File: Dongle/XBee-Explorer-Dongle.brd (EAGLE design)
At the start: 40.6 x 27.9 mm, 26 parts, among them U1 FT232RL-BASICSSOP, U2 XBEE-1B3, U3 V_REG_LDOSMD

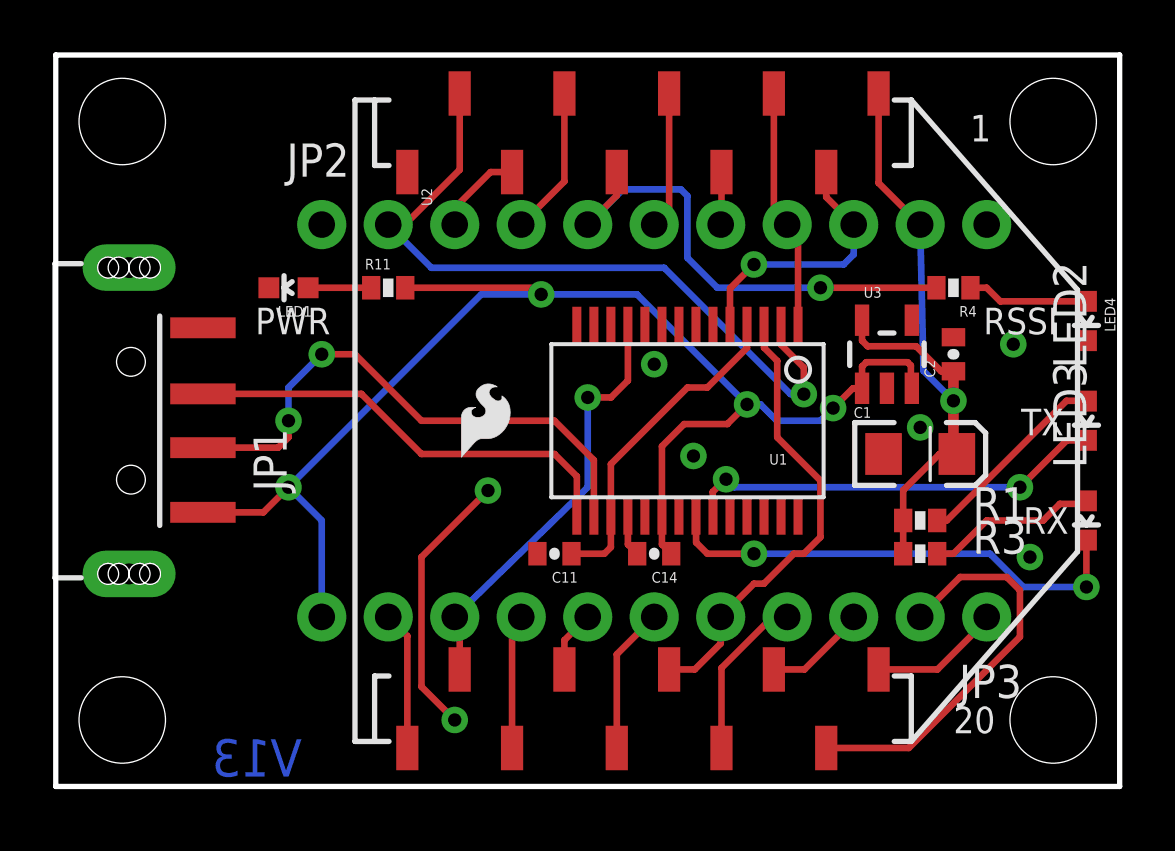
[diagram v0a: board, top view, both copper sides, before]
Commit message: XBee Dongle transition to FT231X
FT231X replaces the FT232RL.
Additional components added (R2, R5, C3, C4).
Updated all resistor and capacitor packages to 0603 footprints.
Rearranged Vreg circuit layout.
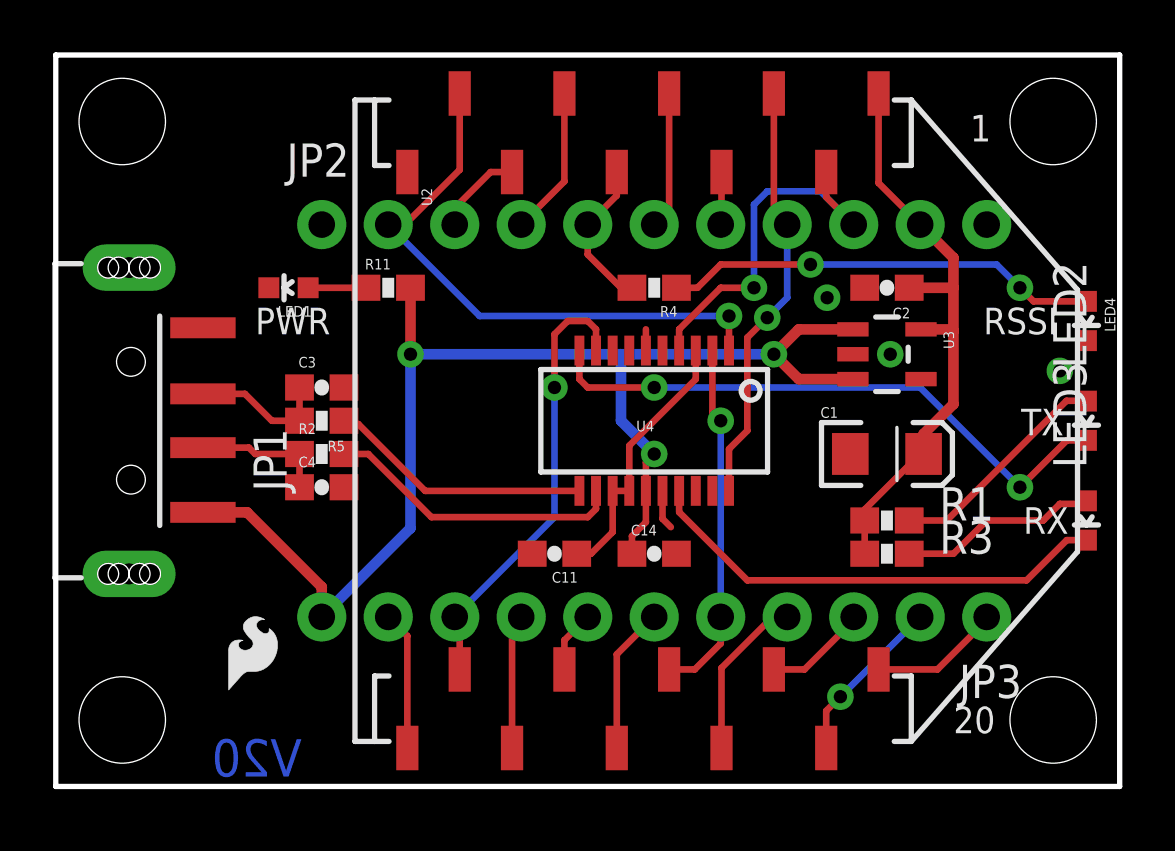
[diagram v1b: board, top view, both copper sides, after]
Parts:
- removed U1: FT232RL-BASICSSOP, SparkFun:SSOP28DB
- added C3, C4: 47pF, SparkFun:0603-CAP
- added R2, R5: 27, SparkFun:0603-RES
- added U4: FT231XS, SparkFun-DigitalIC:SSOP20_L
- C11, C14, C2: device SparkFun:0402-CAP -> SparkFun:0603-CAP
- LED2: value Red -> Red-TX
- LED3: value Green -> Green-RX
- R1, R11, R3, R4: device SparkFun:0402-RES -> SparkFun:0603-RES
- moved U$1 12.6 mm to (6.60, 3.68)
- moved R4 11.4 mm to (22.9, 19.1)
- moved C2 3.59 mm to (31.8, 19.1), turned to 180 degrees
- moved C1 1.27 mm to (31.8, 12.7)
- moved R1 1.27 mm to (31.8, 10.2)
- moved R3 1.27 mm to (31.8, 8.89)
- turned C14 to 0 degrees
- turned U3 to 270 degrees
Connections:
- new net N$5: R2.2, U4.12
- new net N$6: C3.1, JP1.D+1, R5.2
- net 3V-INT: now also U4.13, U4.14, U4.3; no longer U1.17, U1.4
- net 5V: now also U4.15; no longer U1.20
- net CTS: now also U4.9; no longer U1.11
- net DIN: now also U4.20; no longer U1.1
- net DOUT: now also U4.4; no longer U1.5
- net DTR: now also U4.1; no longer U1.2
- net GND: now also C3.2, C4.2, U4.16, U4.6; no longer U1.18, U1.21, U1.25, U1.26, U1.7
- net N$3: now also C4.1, R2.1; no longer U1.16
- net N$7: now also R5.1, U4.11; no longer JP1.D+1, U1.15
- net RTS: now also U4.2; no longer U1.3
- net RXLED: now also U4.17; no longer U1.22
- net TXLED: now also U4.10; no longer U1.23
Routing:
- net N$3: track 21.4 -> 5.06 mm, vias 2 -> 0
- net RSSI: track 19.3 -> 5.83 mm, vias 1 -> 0
- net N$2: track 4.65 -> 16.6 mm, vias 0 -> 2
- net N$5: track 0.00 -> 11.4 mm
- net GND: track 11.9 -> 2.33 mm, vias 7 -> 3
- net DIO1: track 15.6 -> 6.49 mm, vias 0 -> 1
- net N$7: track 17.2 -> 10.1 mm
- net DIN: track 9.23 -> 16.3 mm, vias 0 -> 1
- net TXLED: track 16.3 -> 22.9 mm
- net DTR: track 28.1 -> 22.3 mm
- net N$6: track 0.00 -> 5.38 mm
- net DOUT: track 10.2 -> 14.5 mm
- net RTS: track 17.5 -> 13.7 mm, vias 0 -> 1
- net 5V: track 53.8 -> 50.0 mm, vias 4 -> 3
- net 3.3V: track 26.0 -> 23.2 mm, vias 1 -> 0
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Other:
- board text added: "V20"
- board text removed: "V13"

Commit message: Spaced out resistors and capacitors a tad
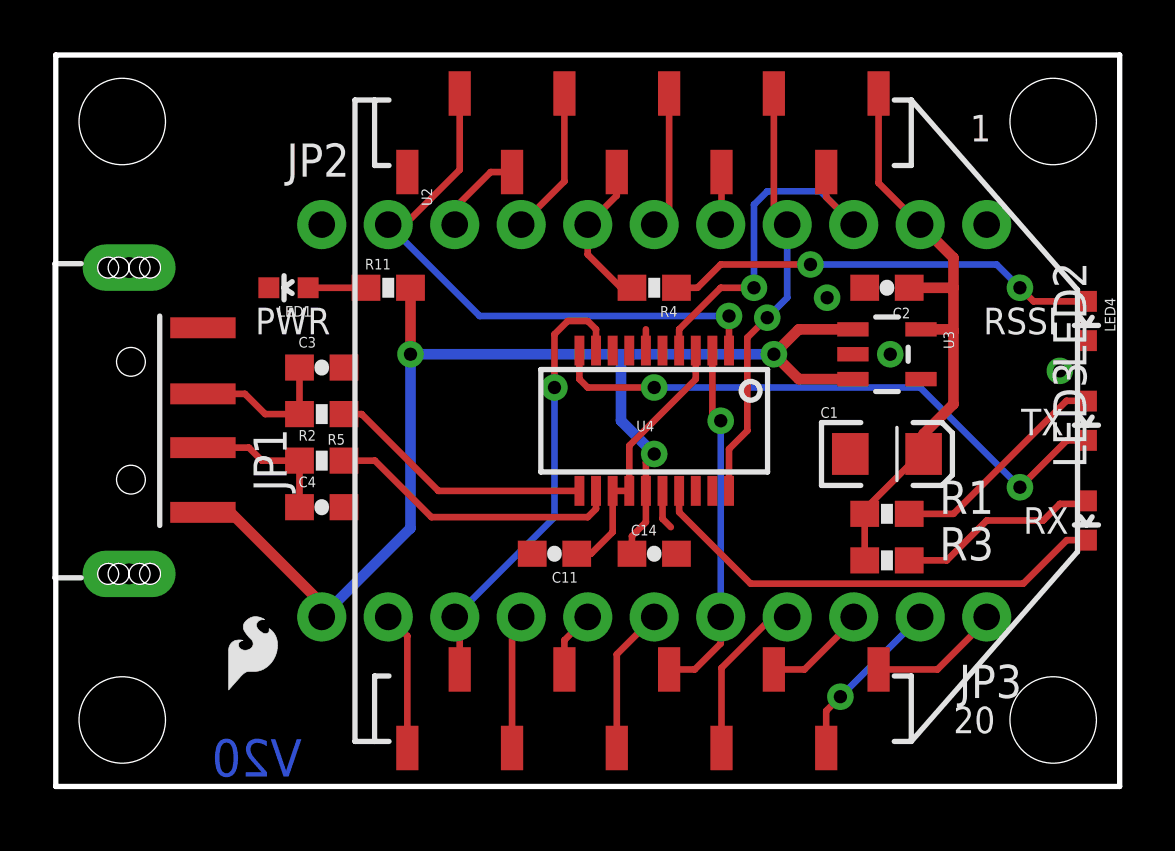
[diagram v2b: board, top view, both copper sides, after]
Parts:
- moved C4 0.76 mm to (10.2, 10.7)
- moved C3 0.76 mm to (10.2, 16.0)
- moved R3 0.25 mm to (31.8, 8.64)
- moved R1 0.25 mm to (31.8, 10.4)
- moved R2 0.25 mm to (10.2, 12.4)
- moved R5 0.25 mm to (10.2, 14.2)
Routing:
- net N$3: track 5.06 -> 5.67 mm
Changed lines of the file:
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@@
 <attribute name="VALUE" x="38.608" y="10.732" size="0.4064" layer="27" rot="R90"/>
 </element>
-<element name="R1" library="SparkFun" package="0603-RES" value="1K" x="31.75" y="10.16" smashed="yes">
-<attribute name="NAME" x="33.75" y="10.16" size="1.27" layer="25"/>
-<attribute name="VALUE" x="29.845" y="10.033" size="0.4064" layer="27"/>
-</element>
-<element name="R3" library="SparkFun" package="0603-RES" value="1K" x="31.75" y="8.89" smashed="yes">
-<attribute name="NAME" x="33.75" y="8.89" size="1.27" layer="25"/>
-<attribute name="VALUE" x="29.845" y="8.763" size="0.4064" layer="27"/>
+<element name="R1" library="SparkFun" package="0603-RES" value="1K" x="31.75" y="10.414" smashed="yes">
+<attribute name="NAME" x="33.75" y="10.414" size="1.27" layer="25"/>
+<attribute name="VALUE" x="29.845" y="10.287" size="0.4064" layer="27"/>
+</element>
+<element name="R3" library="SparkFun" package="0603-RES" value="1K" x="31.75" y="8.636" smashed="yes">
+<attribute name="NAME" x="33.75" y="8.636" size="1.27" layer="25"/>
+<attribute name="VALUE" x="29.845" y="8.509" size="0.4064" layer="27"/>
 </element>
 <element name="U$1" library="SparkFun" package="SFE-LOGO-FLAME" value="LOGO-SFESK" x="6.604" y="3.683"/>
@@
 <element name="JP1" library="SparkFun-Connectors" package="USB-A-SMT-MALE" value="USBA-SMD-MALE" x="2.54" y="13.97" rot="R90"/>
 <element name="U4" library="SparkFun-DigitalIC" package="SSOP20_L" value="FT231XS" x="22.86" y="13.97" rot="R180"/>
-<element name="R2" library="SparkFun" package="0603-RES" value="27" x="10.16" y="12.7"/>
-<element name="R5" library="SparkFun" package="0603-RES" value="27" x="10.16" y="13.97" rot="R180"/>
-<element name="C3" library="SparkFun" package="0603-CAP" value="47pF" x="10.16" y="15.24"/>
-<element name="C4" library="SparkFun" package="0603-CAP" value="47pF" x="10.16" y="11.43"/>
+<element name="R2" library="SparkFun" package="0603-RES" value="27" x="10.16" y="12.446"/>
+<element name="R5" library="SparkFun" package="0603-RES" value="27" x="10.16" y="14.224" rot="R180"/>
+<element name="C3" library="SparkFun" package="0603-CAP" value="47pF" x="10.16" y="16.002"/>
+<element name="C4" library="SparkFun" package="0603-CAP" value="47pF" x="10.16" y="10.668"/>
 </elements>
 <signals>
@@
 <wire x1="22.01" y1="9.564" x2="22.5425" y2="10.0965" width="0.254" layer="1"/>
 <wire x1="22.5425" y1="11.2903" x2="22.5425" y2="10.0965" width="0.254" layer="1"/>
-<wire x1="5.6218" y1="10.47" x2="7.31" y2="10.47" width="0.4064" layer="1"/>
-<wire x1="7.31" y1="10.47" x2="10.16" y2="7.62" width="0.4064" layer="1"/>
-<wire x1="10.16" y1="7.62" x2="10.16" y2="6.477" width="0.4064" layer="1"/>
+<wire x1="5.6218" y1="10.47" x2="6.675" y2="10.47" width="0.4064" layer="1"/>
+<wire x1="6.675" y1="10.47" x2="10.16" y2="6.985" width="0.4064" layer="1"/>
+<wire x1="10.16" y1="6.985" x2="10.16" y2="6.477" width="0.4064" layer="1"/>
 <wire x1="13.55" y1="19.05" x2="13.55" y2="16.51" width="0.4064" layer="1"/>
 <via x="13.55" y="16.51" extent="1-16" drill="0.508"/>
@@
 <wire x1="39.37" y1="14.732" x2="39.37" y2="14.72" width="0.254" layer="1"/>
 <wire x1="38.608" y1="14.732" x2="39.37" y2="14.732" width="0.254" layer="1"/>
-<wire x1="34.036" y1="10.16" x2="38.608" y2="14.732" width="0.254" layer="1"/>
-<wire x1="32.6" y1="10.16" x2="34.036" y2="10.16" width="0.254" layer="1"/>
+<wire x1="34.29" y1="10.414" x2="38.608" y2="14.732" width="0.254" layer="1"/>
+<wire x1="32.6" y1="10.414" x2="34.29" y2="10.414" width="0.254" layer="1"/>
 </signal>
 <signal name="N$4">
@@
 <wire x1="39.37" y1="10.795" x2="39.37" y2="10.91" width="0.254" layer="1"/>
 <wire x1="38.354" y1="10.795" x2="39.37" y2="10.795" width="0.254" layer="1"/>
-<wire x1="32.6" y1="8.89" x2="34.29" y2="8.89" width="0.254" layer="1"/>
+<wire x1="32.6" y1="8.636" x2="34.036" y2="8.636" width="0.254" layer="1"/>
 <wire x1="37.719" y1="10.16" x2="35.56" y2="10.16" width="0.254" layer="1"/>
-<wire x1="35.56" y1="10.16" x2="34.29" y2="8.89" width="0.254" layer="1"/>
+<wire x1="35.56" y1="10.16" x2="34.036" y2="8.636" width="0.254" layer="1"/>
 </signal>
 <signal name="DIN">
@@
 <contactref element="R3" pad="1"/>
 <contactref element="R1" pad="1"/>
-<wire x1="30.9" y1="10.16" x2="30.9" y2="8.89" width="0.254" layer="1"/>
-<wire x1="30.9" y1="10.16" x2="30.9" y2="10.58" width="0.254" layer="1"/>
+<wire x1="30.9" y1="10.414" x2="30.9" y2="8.636" width="0.254" layer="1"/>
+<wire x1="30.9" y1="10.414" x2="30.9" y2="10.58" width="0.254" layer="1"/>
 <wire x1="33.15" y1="12.7" x2="33.02" y2="12.7" width="0.254" layer="1"/>
 <wire x1="33.02" y1="12.7" x2="30.9" y2="10.58" width="0.254" layer="1"/>
@@
 <contactref element="U4" pad="17"/>
 <wire x1="23.8125" y1="11.2903" x2="23.8125" y2="10.4775" width="0.254" layer="1"/>
-<wire x1="23.8125" y1="10.4775" x2="26.416" y2="7.874" width="0.254" layer="1"/>
-<wire x1="26.416" y1="7.874" x2="37.084" y2="7.874" width="0.254" layer="1"/>
-<wire x1="37.084" y1="7.874" x2="38.62" y2="9.41" width="0.254" layer="1"/>
+<wire x1="23.8125" y1="10.4775" x2="26.543" y2="7.747" width="0.254" layer="1"/>
+<wire x1="26.543" y1="7.747" x2="36.957" y2="7.747" width="0.254" layer="1"/>
+<wire x1="36.957" y1="7.747" x2="38.62" y2="9.41" width="0.254" layer="1"/>
 <wire x1="39.37" y1="9.41" x2="38.62" y2="9.41" width="0.254" layer="1"/>
 </signal>
@@
 <contactref element="C4" pad="1"/>
 <wire x1="5.6218" y1="12.943" x2="7.377" y2="12.943" width="0.254" layer="1"/>
-<wire x1="7.377" y1="12.943" x2="7.62" y2="12.7" width="0.254" layer="1"/>
-<wire x1="7.62" y1="12.7" x2="9.31" y2="12.7" width="0.254" layer="1"/>
-<wire x1="9.31" y1="11.43" x2="9.31" y2="12.7" width="0.254" layer="1"/>
+<wire x1="7.377" y1="12.943" x2="7.874" y2="12.446" width="0.254" layer="1"/>
+<wire x1="7.874" y1="12.446" x2="9.31" y2="12.446" width="0.254" layer="1"/>
+<wire x1="9.31" y1="10.668" x2="9.31" y2="12.446" width="0.254" layer="1"/>
 </signal>
 <signal name="N$5">
 <contactref element="R2" pad="2"/>
 <contactref element="U4" pad="12"/>
-<wire x1="11.01" y1="12.7" x2="11.938" y2="12.7" width="0.254" layer="1"/>
-<wire x1="11.938" y1="12.7" x2="14.351" y2="10.287" width="0.254" layer="1"/>
+<wire x1="11.01" y1="12.446" x2="12.192" y2="12.446" width="0.254" layer="1"/>
+<wire x1="12.192" y1="12.446" x2="14.351" y2="10.287" width="0.254" layer="1"/>
 <wire x1="14.351" y1="10.287" x2="20.32" y2="10.287" width="0.254" layer="1"/>
 <wire x1="20.32" y1="10.287" x2="20.6375" y2="10.6045" width="0.254" layer="1"/>
@@
 <contactref element="R5" pad="2"/>
 <contactref element="C3" pad="1"/>
-<wire x1="9.31" y1="13.97" x2="9.31" y2="15.24" width="0.254" layer="1"/>
+<wire x1="9.31" y1="14.224" x2="9.31" y2="16.002" width="0.254" layer="1"/>
 <wire x1="5.6218" y1="14.997" x2="7.228" y2="14.997" width="0.254" layer="1"/>
-<wire x1="7.228" y1="14.997" x2="8.255" y2="13.97" width="0.254" layer="1"/>
-<wire x1="8.255" y1="13.97" x2="9.31" y2="13.97" width="0.254" layer="1"/>
+<wire x1="7.228" y1="14.997" x2="8.001" y2="14.224" width="0.254" layer="1"/>
+<wire x1="8.001" y1="14.224" x2="9.31" y2="14.224" width="0.254" layer="1"/>
 </signal>
 <signal name="N$7">
 <contactref element="R5" pad="1"/>
 <contactref element="U4" pad="11"/>
-<wire x1="11.01" y1="13.97" x2="11.557" y2="13.843" width="0.254" layer="1"/>
-<wire x1="11.557" y1="13.843" x2="14.1097" y2="11.2903" width="0.254" layer="1"/>
-<wire x1="20.0025" y1="11.2903" x2="14.1097" y2="11.2903" width="0.254" layer="1"/>
+<wire x1="11.01" y1="14.224" x2="11.684" y2="14.224" width="0.254" layer="1"/>
+<wire x1="11.684" y1="14.224" x2="14.6177" y2="11.2903" width="0.254" layer="1"/>
+<wire x1="20.0025" y1="11.2903" x2="14.6177" y2="11.2903" width="0.254" layer="1"/>
 </signal>
 </signals>
+<errors>
+</errors>
 </board>
 </drawing>
